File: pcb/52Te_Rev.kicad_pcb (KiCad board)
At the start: 2 copper layers, 159.1 x 145.6 mm, 64 parts, among them J1 MJ-4PP-9, J2 Conn_01x04, SW1 SW_PUSH, SW10 SW_PUSH, SW11 SW_PUSH, SW12 SW_PUSH, SW13 SW_PUSH, SW14 SW_PUSH, SW15 SW_PUSH, SW16 SW_PUSH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

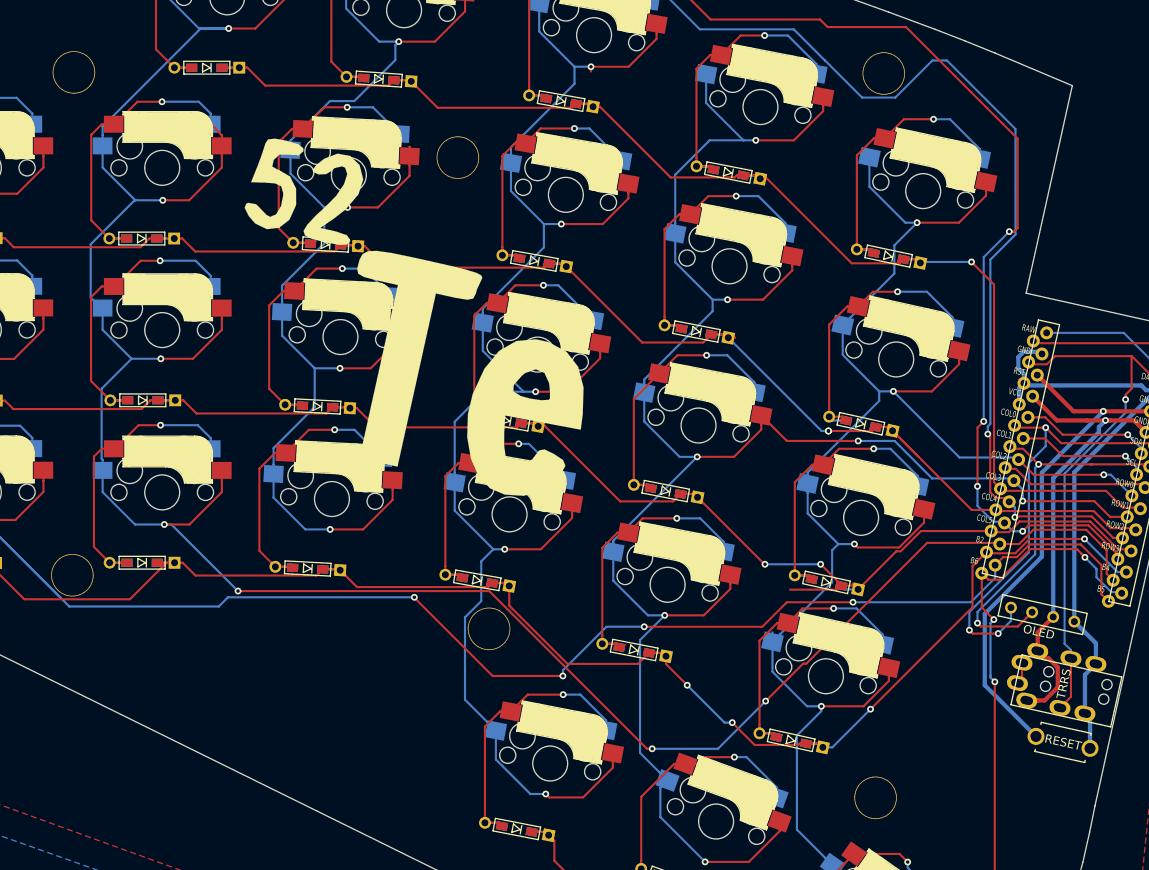
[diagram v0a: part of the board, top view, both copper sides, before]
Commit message: fixed PCB TRRS jack connection
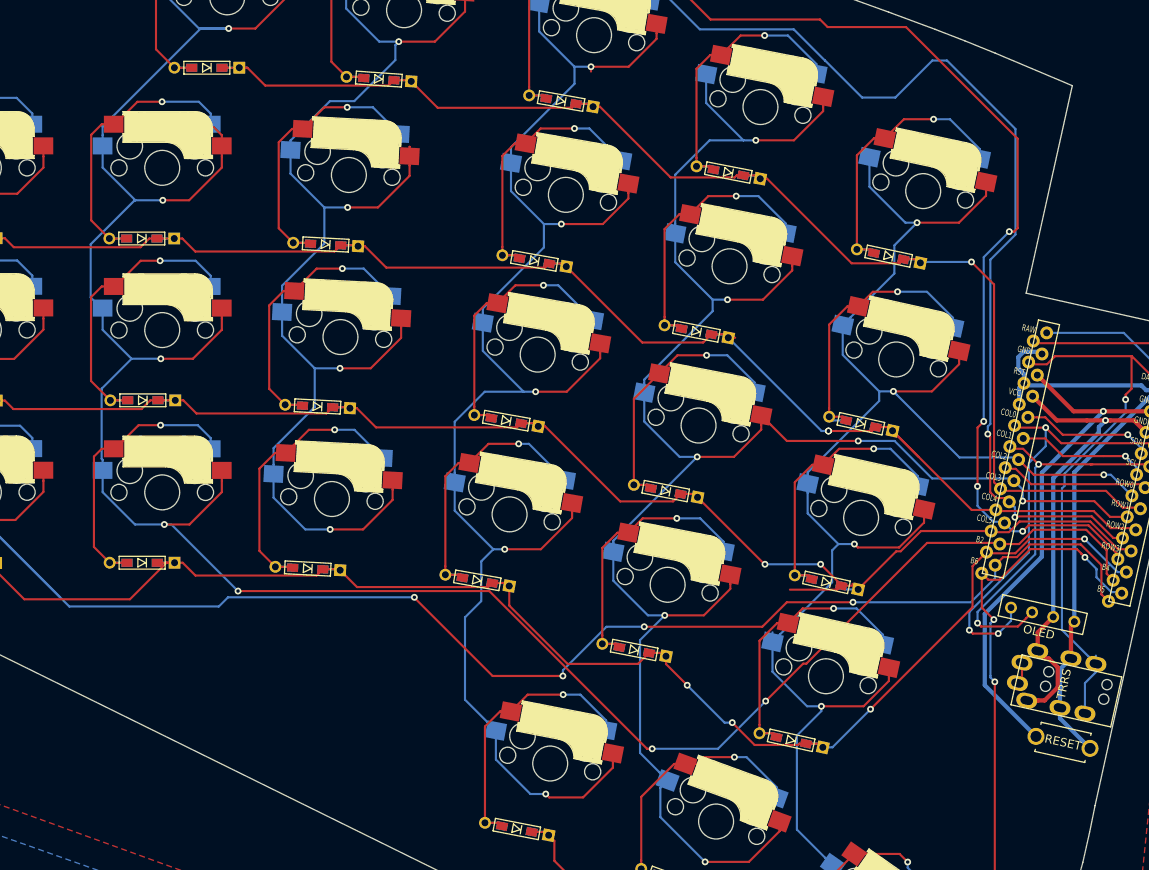
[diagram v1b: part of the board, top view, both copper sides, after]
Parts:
- removed G***: LOGO, 52Te_Rev:emptystringLogo
- removed G***: LOGO, 52Te_Rev:52TeLogo
- removed Ref** (x6): Val**, kbd:HOLE
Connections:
- J1 pad B: GND -> data
- J1 pad C: data -> GND
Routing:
- net data: track 63.6 -> 68.4 mm

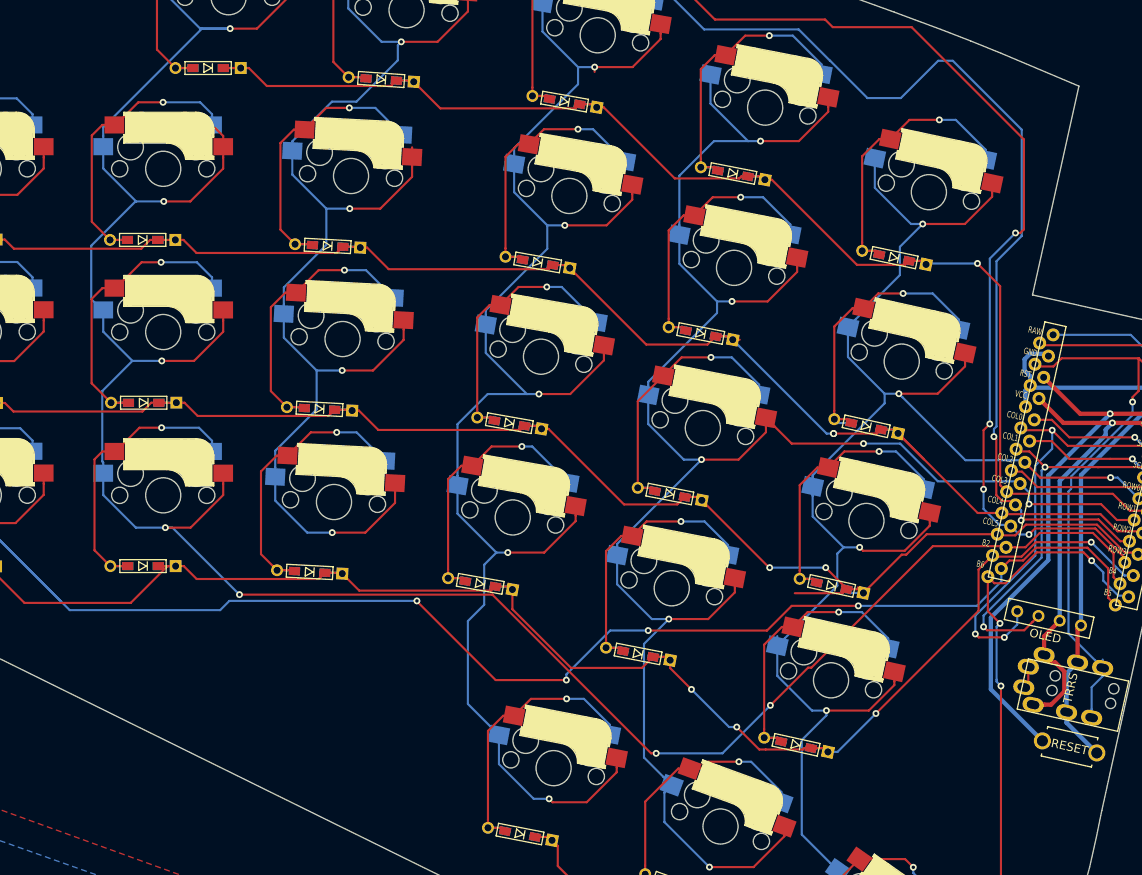
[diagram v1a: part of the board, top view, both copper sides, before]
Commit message: added screw holes back, new gerber
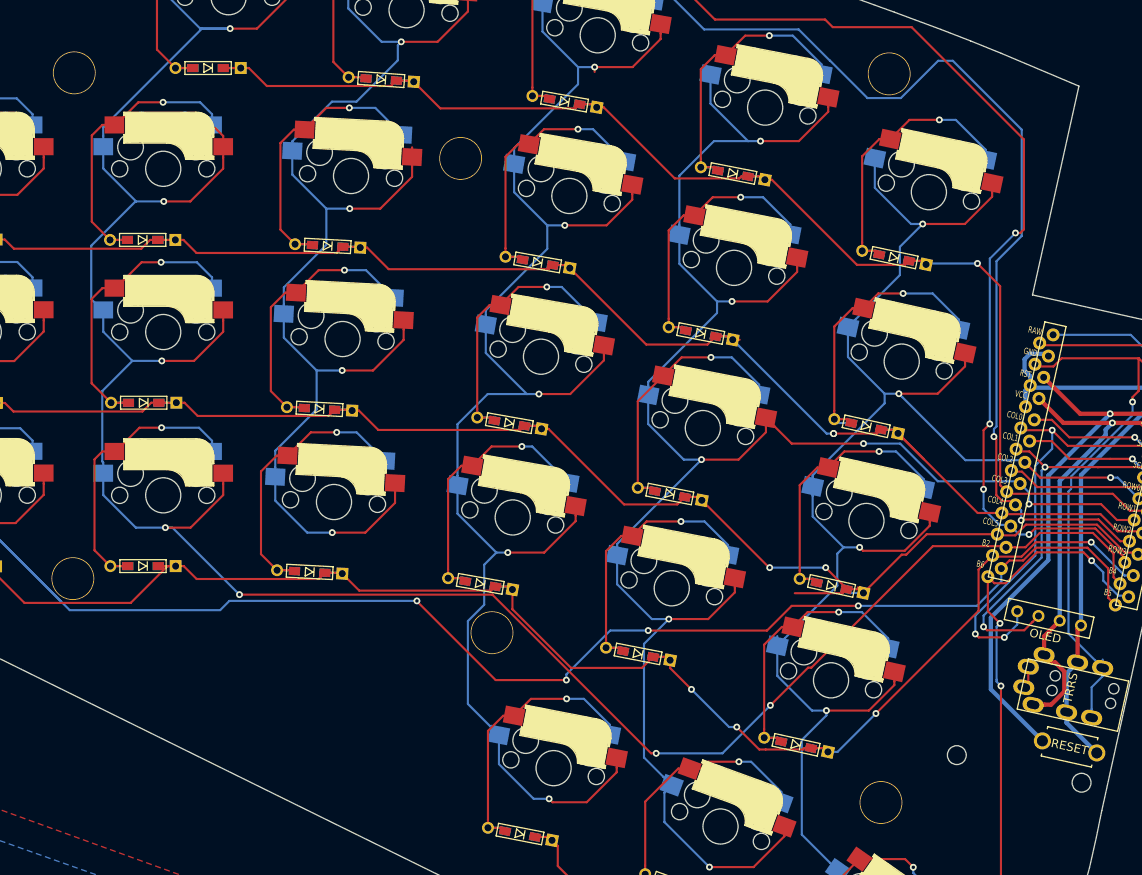
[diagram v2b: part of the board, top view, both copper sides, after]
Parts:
- added ?: MountingHole_2.2mm_M2, MountingHole:MountingHole_2.2mm_M2, F.Cu at (252.6, 177.7)
- added ?: MountingHole_2.2mm_M2, MountingHole:MountingHole_2.2mm_M2, F.Cu at (267.2, 181.0)
- added Ref**: Val**, kbd:HOLE, F.Cu at (149.6, 98.1)
- added Ref**: Val**, kbd:HOLE, F.Cu at (149.4, 157.1)
- added Ref**: Val**, kbd:HOLE, F.Cu at (198.3, 163.4)
- added Ref**: Val**, kbd:HOLE, F.Cu at (243.8, 183.3)
- added Ref**: Val**, kbd:HOLE, F.Cu at (194.7, 108.1)
- added Ref**: Val**, kbd:HOLE, F.Cu at (244.7, 98.2)

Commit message: added logos
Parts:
- added G***: LOGO, 52Te_Rev:emptystringLogo, B.Cu at (179.9, 133.7)
- added G***: LOGO, 52Te_Rev:52TeLogo, F.Cu at (191.2, 128.8)

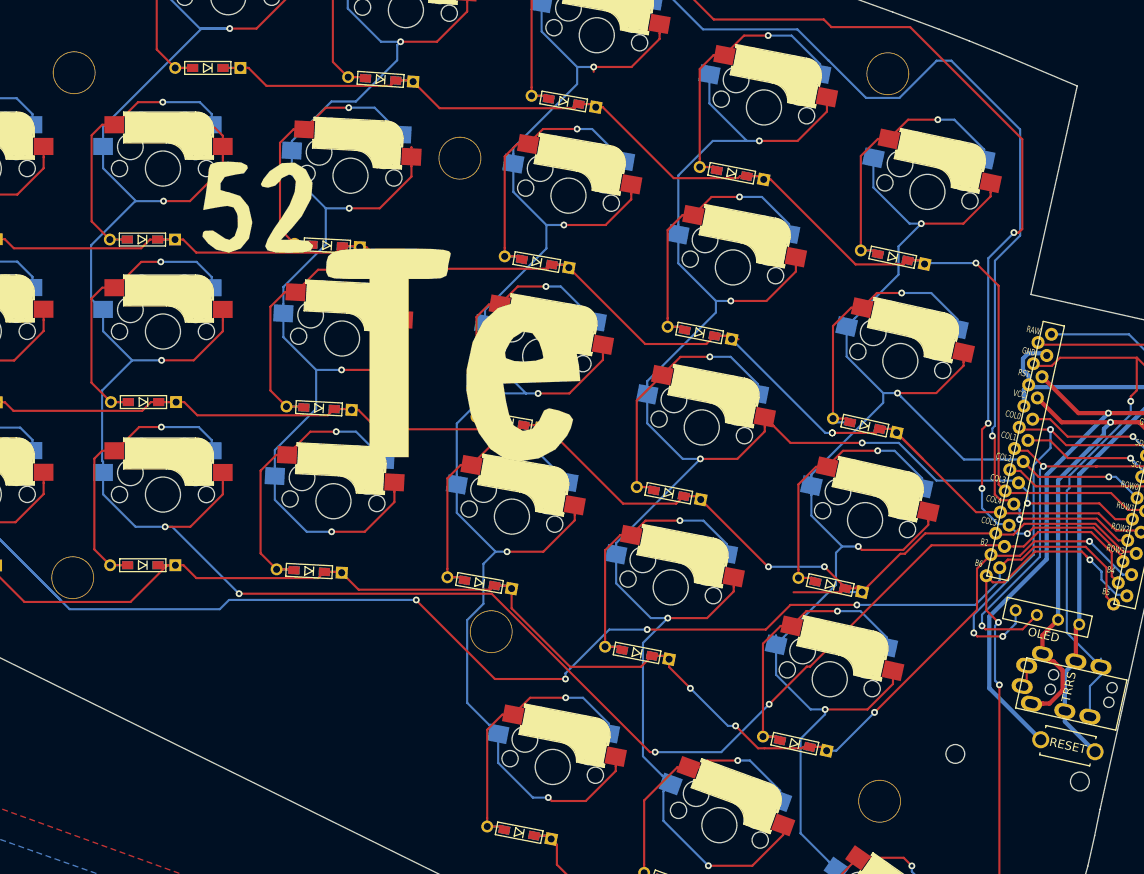
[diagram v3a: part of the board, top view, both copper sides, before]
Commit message: removed OLED footprints
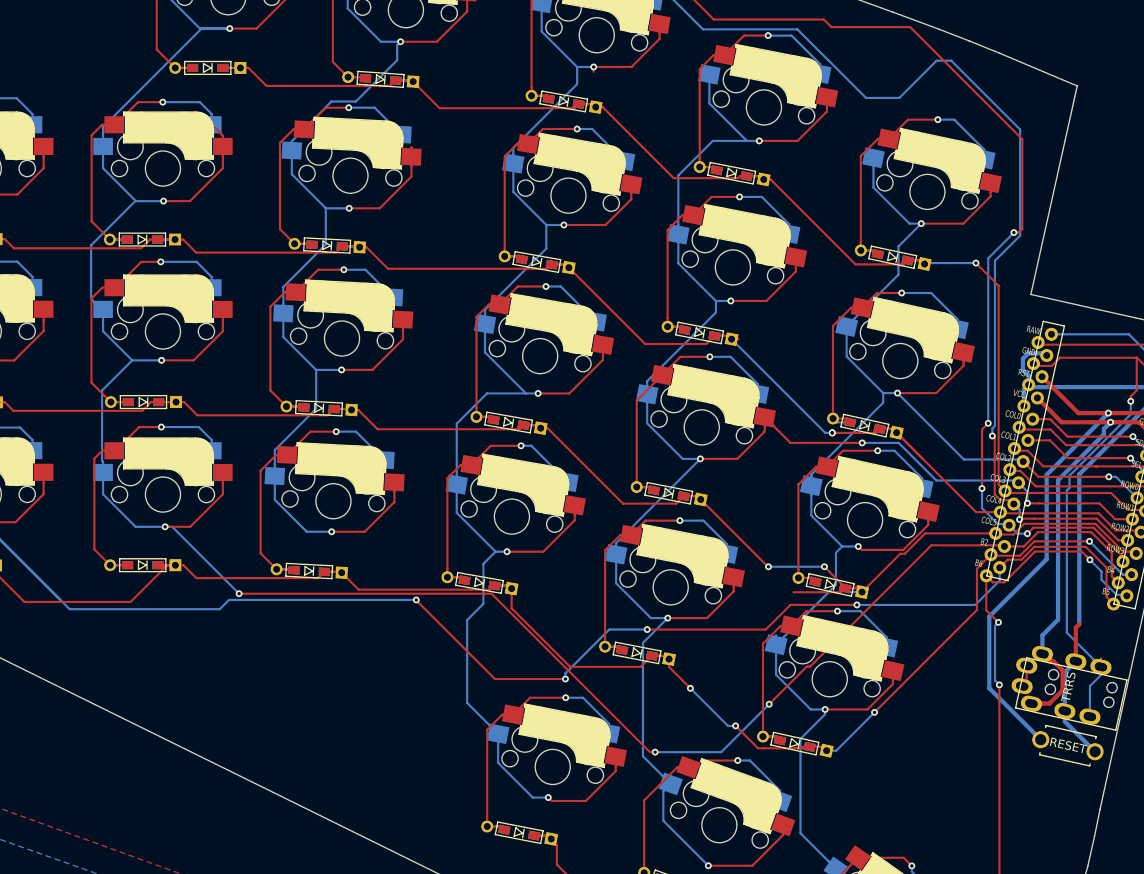
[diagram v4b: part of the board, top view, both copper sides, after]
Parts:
- removed ? (x2): MountingHole_2.2mm_M2, MountingHole:MountingHole_2.2mm_M2
- removed G***: LOGO, 52Te_Rev:emptystringLogo
- removed G***: LOGO, 52Te_Rev:52TeLogo
- removed J2: Conn_01x04, kbd:OLED
- removed Ref** (x6): Val**, kbd:HOLE
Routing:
- net SDA: track 52.1 -> 17.4 mm, vias 3 -> 0
- net SCL: track 46.5 -> 17.6 mm, vias 2 -> 0

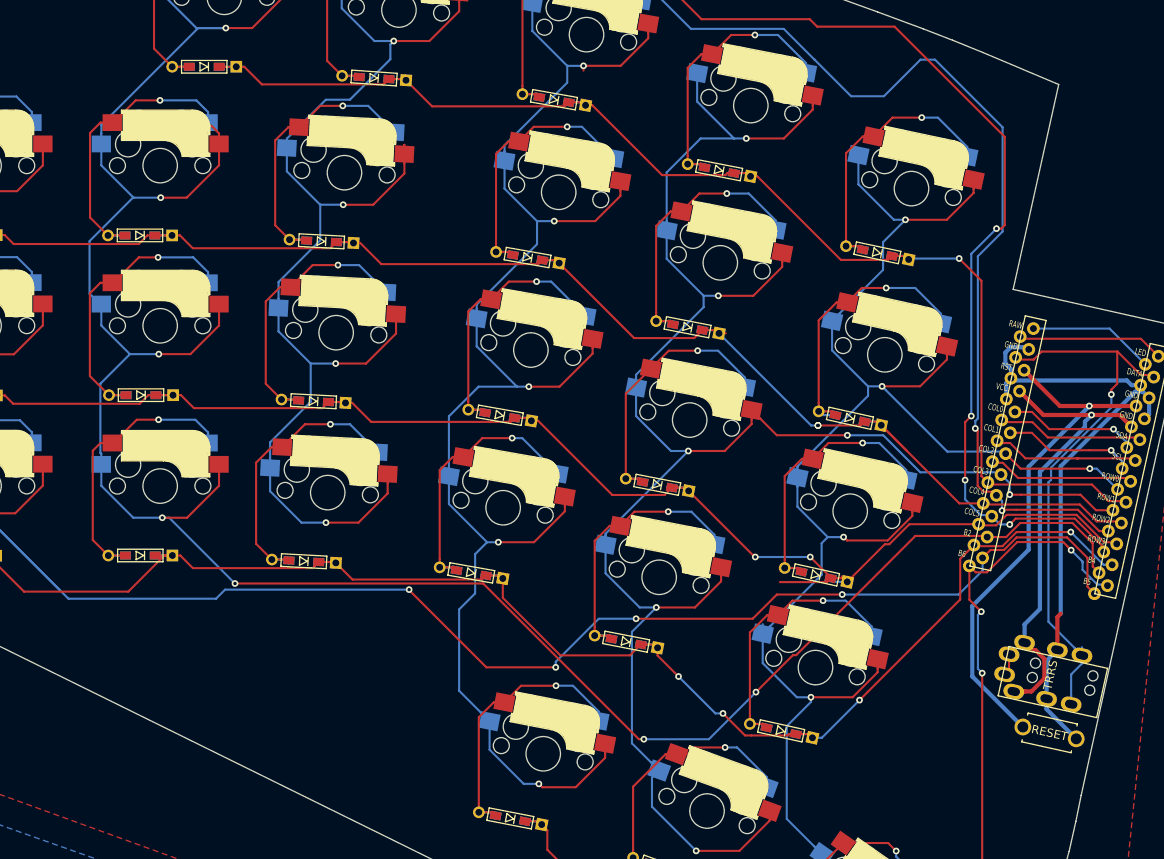
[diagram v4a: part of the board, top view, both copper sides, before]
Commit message: added holes and redid routing around trrs/reset
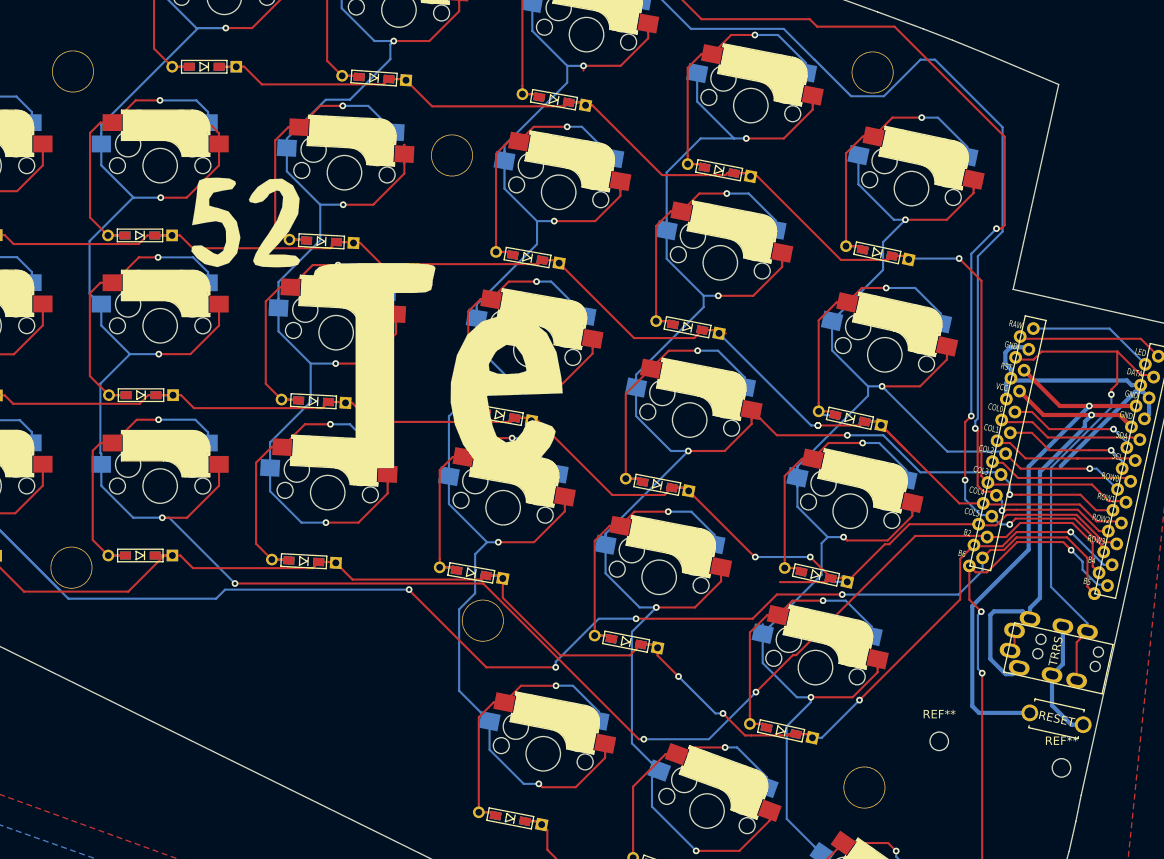
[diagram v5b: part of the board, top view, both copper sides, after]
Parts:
- added G***: LOGO, emptystring:52TeLogo, F.Cu at (190.3, 131.1)
- added G***: LOGO, emptystring:emptystringLogo, B.Cu at (195.7, 136.1)
- added REF**: MountingHole_2.2mm_M2, MountingHole:MountingHole_2.2mm_M2, F.Cu at (252.6, 177.8)
- added REF**: MountingHole_2.2mm_M2, MountingHole:MountingHole_2.2mm_M2, F.Cu at (267.2, 180.9)
- added Ref**: Val**, kbd:HOLE, F.Cu at (149.6, 98.1)
- added Ref**: Val**, kbd:HOLE, F.Cu at (149.4, 157.1)
- added Ref**: Val**, kbd:HOLE, F.Cu at (194.7, 108.1)
- added Ref**: Val**, kbd:HOLE, F.Cu at (198.4, 163.4)
- added Ref**: Val**, kbd:HOLE, F.Cu at (243.7, 183.3)
- added Ref**: Val**, kbd:HOLE, F.Cu at (244.7, 98.2)
- moved J1 2.90 mm to (272.7, 169.2)
- moved SW27 1.87 mm to (266.6, 175.1)
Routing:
- net GND: track 79.0 -> 58.1 mm
- net data: track 68.4 -> 62.9 mm
- net reset: track 61.5 -> 63.7 mm
- net VCC: track 55.2 -> 57.3 mm
- net Net-(J1-PadA): track 2.61 -> 3.36 mm

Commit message: new gerber file
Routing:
- net GND: track 58.1 -> 43.5 mm
- net row2: track 171.7 -> 164.5 mm
- net col1: track 280.4 -> 277.8 mm
- net col5: track 211.2 -> 210.1 mm
- net col2: track 298.3 -> 297.2 mm
- net row0: track 156.4 -> 155.5 mm
- net row1: track 170.7 -> 169.9 mm, vias 2 -> 1
- net (no net): track 0.60 -> 0.00 mm
- net col3: track 313.9 -> 313.4 mm
